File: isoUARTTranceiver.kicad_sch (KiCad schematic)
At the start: 20 parts, among them U2 TLE9015DQUXUMA1

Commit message: tweaked a little
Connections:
- net 3V3: now also C1.1, R1.1, U2.27 (VDDC)
- net 5V: no longer C1.1, C3.1, R1.1, U2.27 (VDDC), U2.30 (VIO)
- net at C2.1, U2.31 (VREGOUT): now also C3.1, U2.30 (VIO)
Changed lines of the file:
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@@
 	)
 	(junction
+		(at 233.68 96.52)
+		(diameter 0)
+		(color 0 0 0 0)
+	)
+	(junction
 		(at 138.43 76.2)
 		(diameter 0)
@@
 	)
 	(junction
-		(at 233.68 104.14)
-		(diameter 0)
-		(color 0 0 0 0)
-	)
-	(junction
 		(at 137.16 142.24)
 		(diameter 0)
@@
 	)
 	(junction
+		(at 233.68 93.98)
+		(diameter 0)
+		(color 0 0 0 0)
+	)
+	(junction
 		(at 138.43 81.28)
 		(diameter 0)
@@
 	(wire
 		(pts
-			(xy 233.68 101.6) (xy 233.68 104.14)
-		)
-		(stroke
-			(width 0)
-			(type default)
-		)
-	)
-	(wire
-		(pts
 			(xy 217.17 81.28) (xy 217.17 82.55)
 		)
@@
 	(wire
 		(pts
-			(xy 228.6 104.14) (xy 233.68 104.14)
-		)
-		(stroke
-			(width 0)
-			(type default)
-		)
-	)
-	(wire
-		(pts
 			(xy 101.6 130.81) (xy 101.6 140.97)
 		)
@@
 	(wire
 		(pts
+			(xy 201.93 93.98) (xy 233.68 93.98)
+		)
+		(stroke
+			(width 0)
+			(type default)
+		)
+	)
+	(wire
+		(pts
 			(xy 133.35 142.24) (xy 137.16 142.24)
 		)
@@
 	(wire
 		(pts
-			(xy 138.43 66.04) (xy 140.97 66.04)
+			(xy 233.68 93.98) (xy 233.68 96.52)
 		)
 		(stroke
@@
 	(wire
 		(pts
-			(xy 101.6 93.98) (xy 101.6 95.25)
+			(xy 138.43 66.04) (xy 140.97 66.04)
 		)
 		(stroke
@@
 	(wire
 		(pts
-			(xy 217.17 66.04) (xy 217.17 68.58)
+			(xy 101.6 93.98) (xy 101.6 95.25)
 		)
 		(stroke
@@
 	(wire
 		(pts
-			(xy 228.6 96.52) (xy 228.6 104.14)
+			(xy 217.17 66.04) (xy 217.17 68.58)
 		)
 		(stroke
@@
 	(wire
 		(pts
-			(xy 201.93 96.52) (xy 228.6 96.52)
+			(xy 201.93 96.52) (xy 233.68 96.52)
 		)
 		(stroke
@@
 	(wire
 		(pts
-			(xy 201.93 93.98) (xy 246.38 93.98)
-		)
-		(stroke
-			(width 0)
-			(type default)
-		)
-	)
-	(wire
-		(pts
 			(xy 138.43 76.2) (xy 138.43 78.74)
 		)
@@
 	(wire
 		(pts
-			(xy 233.68 104.14) (xy 233.68 105.41)
+			(xy 233.68 96.52) (xy 233.68 105.41)
 		)
 		(stroke
@@
 	(wire
 		(pts
+			(xy 233.68 93.98) (xy 246.38 93.98)
+		)
+		(stroke
+			(width 0)
+			(type default)
+		)
+	)
+	(wire
+		(pts
 			(xy 138.43 53.34) (xy 138.43 55.88)
 		)
@@
 		(in_pos_files yes)
 		(dnp no)
-		(fields_autoplaced yes)
 		(property "Reference" "#PWR07"
 			(at 219.71 107.95 0)
@@
 			)
 		)
-		(property "Value" "5V"
-			(at 219.71 99.06 0)
+		(property "Value" "3V3"
+			(at 217.932 99.568 0)
 			(show_name no)
 			(do_not_autoplace no)
@@
 					(size 1.27 1.27)
 				)
+				(justify left)
 			)
 		)
@@
 	)
 	(symbol
-		(lib_id "power:VDDA")
-		(at 233.68 101.6 0)
-		(unit 1)
-		(body_style 1)
-		(exclude_from_sim no)
-		(in_bom yes)
-		(on_board yes)
-		(in_pos_files yes)
-		(dnp no)
-		(fields_autoplaced yes)
-		(property "Reference" "#PWR08"
-			(at 233.68 105.41 0)
-			(hide yes)
-			(show_name no)
-			(do_not_autoplace no)
-			(effects
-				(font
-					(size 1.27 1.27)
-				)
-			)
-		)
-		(property "Value" "5V"
-			(at 233.68 96.52 0)
-			(show_name no)
-			(do_not_autoplace no)
-			(effects
-				(font
-					(size 1.27 1.27)
-				)
-			)
-		)
-		(property "Footprint" ""
-			(at 233.68 101.6 0)
-			(hide yes)
-			(show_name no)
-			(do_not_autoplace no)
-			(effects
-				(font
-					(size 1.27 1.27)
-				)
-			)
-		)
-		(property "Datasheet" ""
-			(at 233.68 101.6 0)
-			(hide yes)
-			(show_name no)
-			(do_not_autoplace no)
-			(effects
-				(font
-					(size 1.27 1.27)
-				)
-			)
-		)
-		(property "Description" "Power symbol creates a global label with name \"VDDA\""
-			(at 233.68 101.6 0)
-			(hide yes)
-			(show_name no)
-			(do_not_autoplace no)
-			(effects
-				(font
-					(size 1.27 1.27)
-				)
-			)
-		)
-		(pin "1"
-		)
-		(instances
-			(project "bms-main"
-				(path "/d7e1c873-142c-4805-8303-47f5b9830fe8/4e7a0d49-6a60-4c8b-a4ed-2f153f3389c3"
-					(reference "#PWR08")
-					(unit 1)
-				)
-			)
-		)
-	)
-	(symbol
 		(lib_id "Device:C_Small")
 		(at 219.71 107.95 0)
@@
 		(in_pos_files yes)
 		(dnp no)
-		(fields_autoplaced yes)
 		(property "Reference" "#PWR02"
 			(at 231.14 86.36 0)
@@
 			)
 		)
-		(property "Value" "5V"
-			(at 231.14 77.47 0)
+		(property "Value" "3V3"
+			(at 229.616 78.74 0)
 			(show_name no)
 			(do_not_autoplace no)
@@
 					(size 1.27 1.27)
 				)
+				(justify left)
 			)
 		)

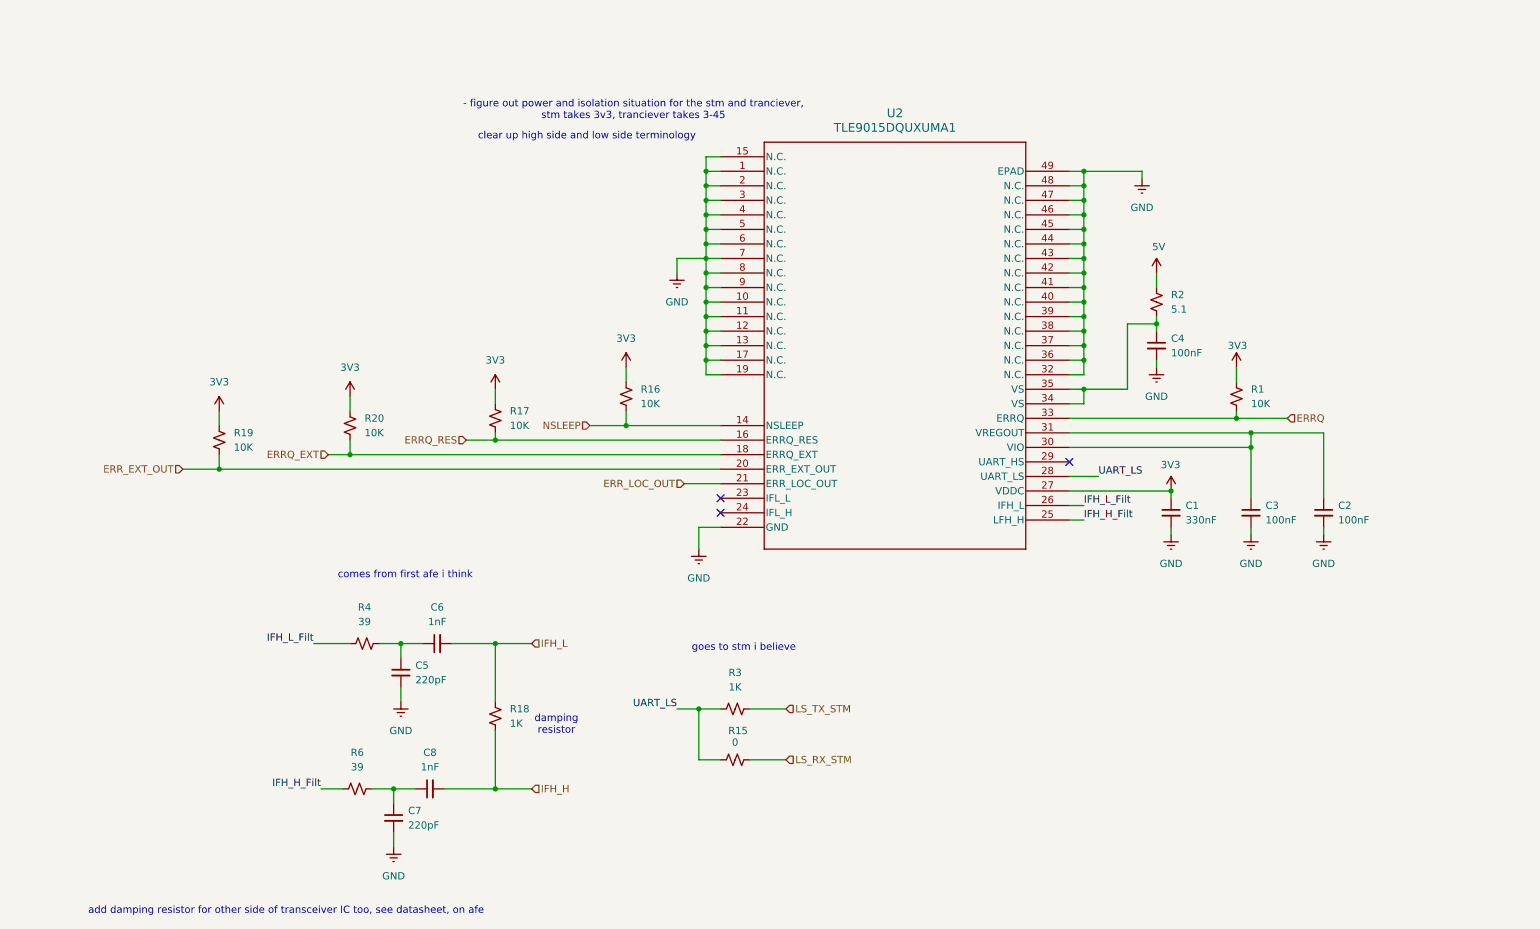
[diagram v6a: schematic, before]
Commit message: added passives
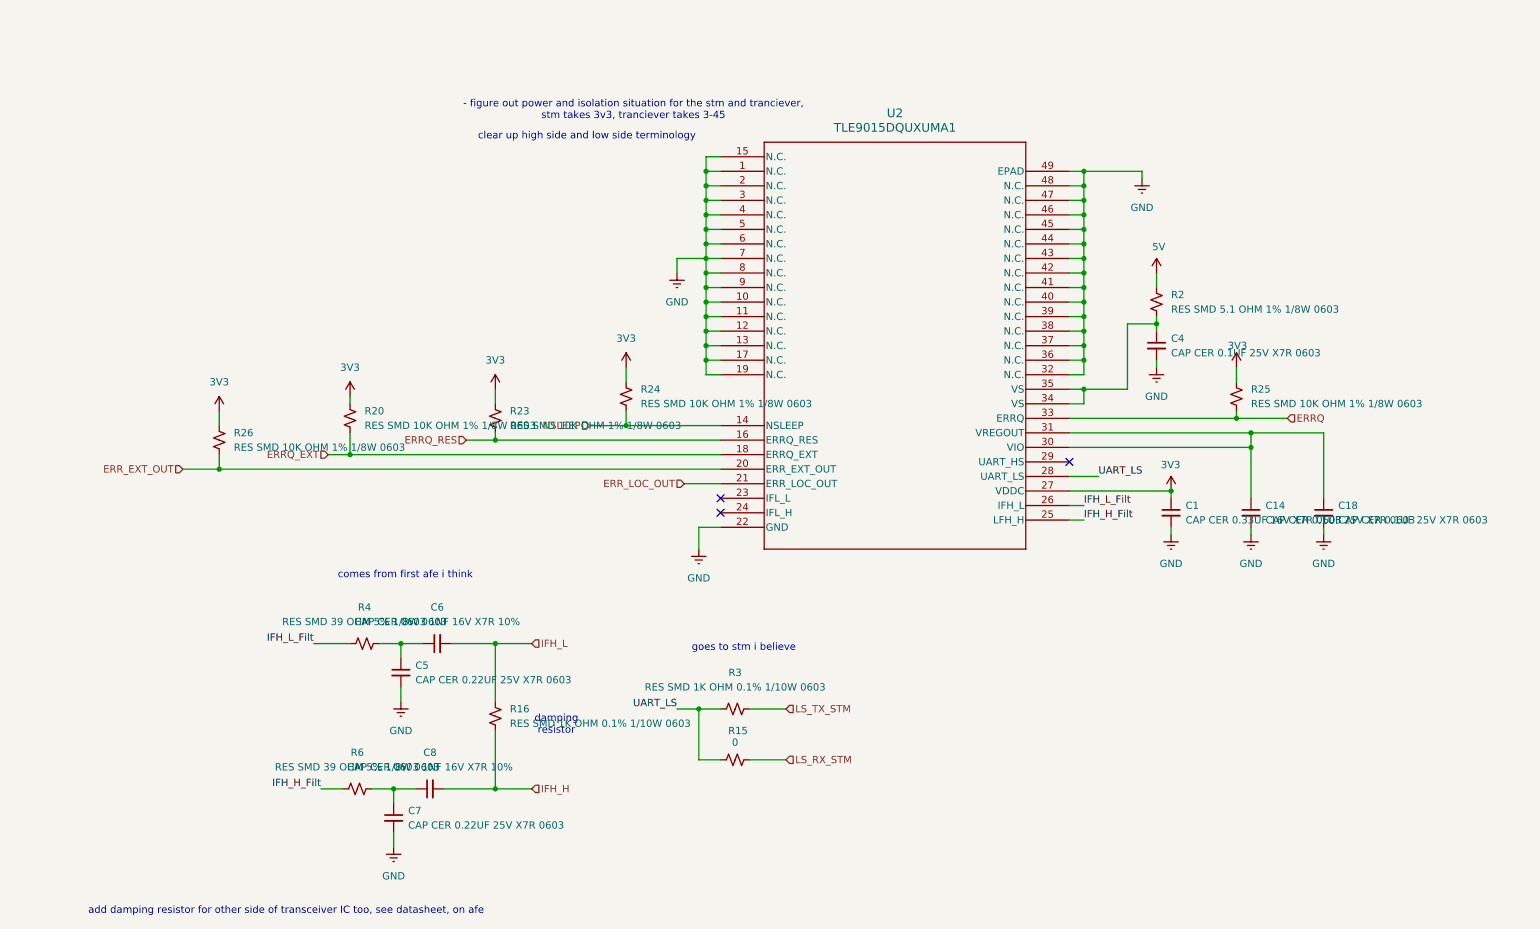
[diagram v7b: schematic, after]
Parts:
- removed C2, C3: 100nF, symbol Device:C_Small
- removed R1, R17, R19: 10K, symbol Device:R_Small_US
- removed R18: 1K, symbol Device:R_Small_US
- added C14, C18: CAP CER 0.1UF 25V X7R 0603, Capacitor_SMD:C_0603_1608Metric, symbol Device:C_Small
- added R23, R24, R25, R26: RES SMD 10K OHM 1% 1/8W 0603, Resistor_SMD:R_0603_1608Metric, symbol Device:R_Small_US
- C1: value 330nF -> CAP CER 0.33UF 16V X7R 0603; footprint (none) -> Capacitor_SMD:C_0603_1608Metric
- C4: value 100nF -> CAP CER 0.1UF 25V X7R 0603; footprint (none) -> Capacitor_SMD:C_0603_1608Metric
- C5, C7: value 220pF -> CAP CER 0.22UF 25V X7R 0603; footprint (none) -> Capacitor_SMD:C_0603_1608Metric
- C6, C8: value 1nF -> CAP CER 0603 1NF 16V X7R 10%; footprint (none) -> Capacitor_SMD:C_0603_1608Metric
- R16: value 10K -> RES SMD 1K OHM 0.1% 1/10W 0603; footprint (none) -> Resistor_SMD:R_0603_1608Metric; LCSC (none) -> C110776
- R2: value 5.1 -> RES SMD 5.1 OHM 1% 1/8W 0603; footprint (none) -> Resistor_SMD:R_0603_1608Metric; LCSC (none) -> C242492
- R20: value 10K -> RES SMD 10K OHM 1% 1/8W 0603; footprint (none) -> Resistor_SMD:R_0603_1608Metric; LCSC (none) -> C844918
- R3: value 1K -> RES SMD 1K OHM 0.1% 1/10W 0603; footprint (none) -> Resistor_SMD:R_0603_1608Metric; LCSC (none) -> C110776
- R4, R6: value 39 -> RES SMD 39 OHM 5% 1/8W 0603; footprint (none) -> Resistor_SMD:R_0603_1608Metric; LCSC (none) -> C2079967
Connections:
- net 3V3: now also R23.1, R24.1, R25.1, R26.1; no longer R16.1
- net ERRQ: now also R25.2
- net ERRQ_RES: now also R23.2
- net ERR_EXT_OUT: now also R26.2
- net GND: now also C14.2, C18.2
- net IFH_H: now also R16.1
- net IFH_L: now also R16.2
- net NSLEEP: now also R24.2; no longer R16.2
- net at U2.30 (VIO), U2.31 (VREGOUT): now also C14.1, C18.1
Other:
- moved on the sheet: R20

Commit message: cleaned up schematic
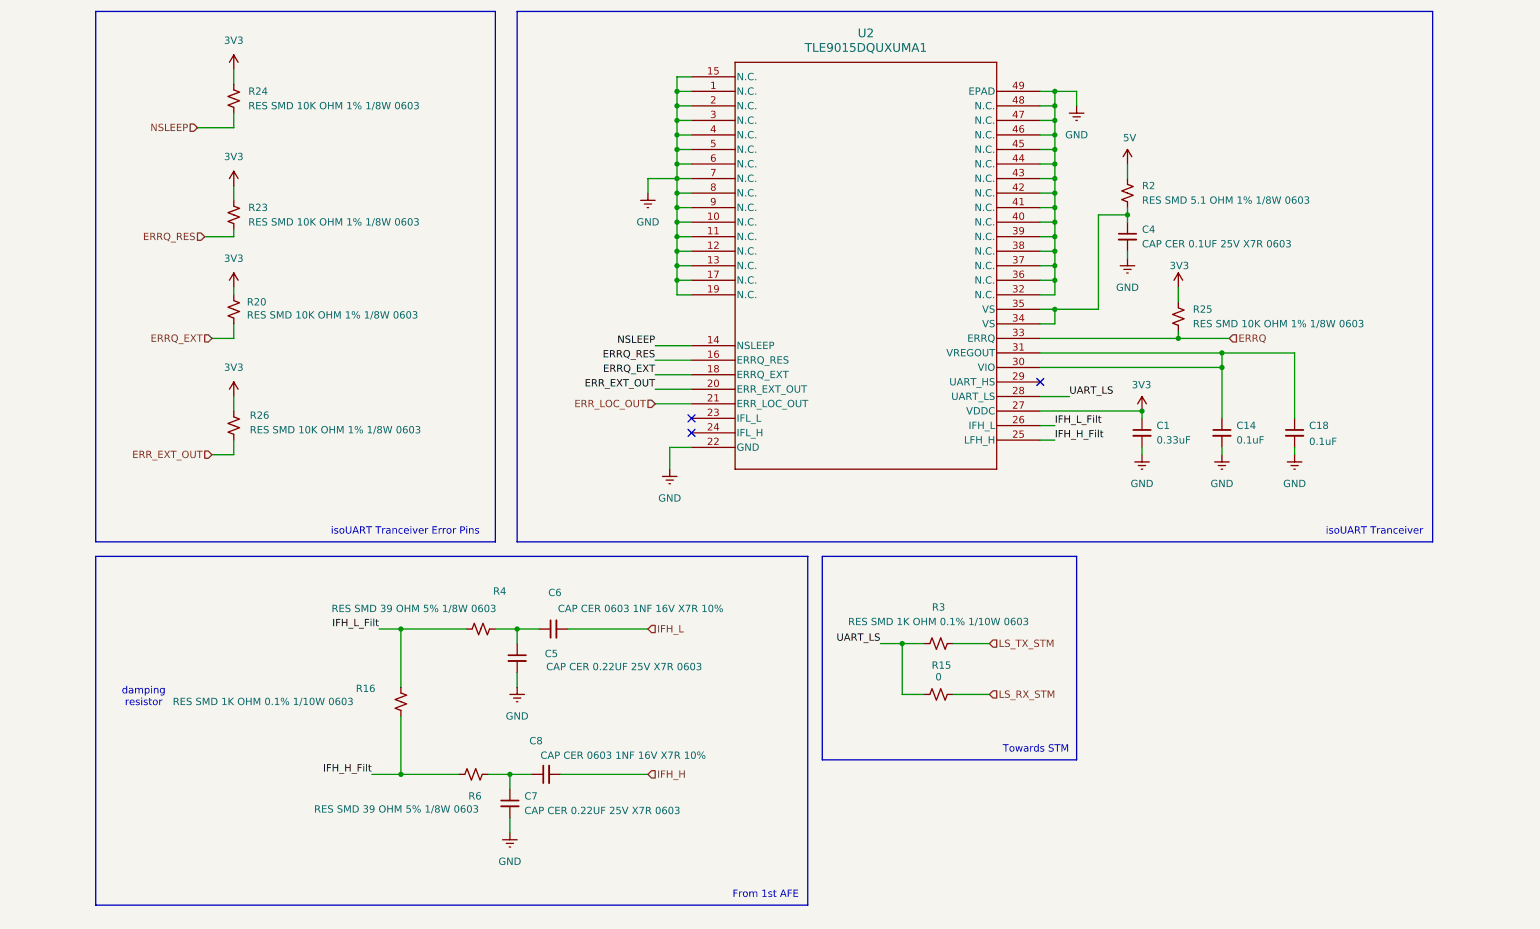
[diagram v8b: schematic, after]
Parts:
- C1: value CAP CER 0.33UF 16V X7R 0603 -> 0.33uF
- C14, C18: value CAP CER 0.1UF 25V X7R 0603 -> 0.1uF
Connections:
- net IFH_H: no longer R16.1
- net IFH_H_Filt: now also R16.1
- net IFH_L: no longer R16.2
- net IFH_L_Filt: now also R16.2
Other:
- note added: "From 1st AFE"
- note added: "Towards STM"
- note added: "isoUART Tranceiver"
- note added: "isoUART Tranceiver Error Pins"
- note removed: "- figure out power and isolation situation for the stm and tranciever, stm takes 3v3, tranciever takes 3-45"
- note removed: "add damping resistor for other side of transceiver IC too, see datasheet, on afe"
- note removed: "clear up high side and low side terminology"
- note removed: "comes from first afe i think"
- note removed: "goes to stm i believe"
- moved on the sheet: C1, C14, C18, C4, C5, C6, C7, C8, R15, R2, R25, R26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
